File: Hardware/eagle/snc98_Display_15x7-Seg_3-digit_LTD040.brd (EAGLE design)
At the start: 154.9 x 33.5 mm, 72 parts, among them M10 IRLML2244, M11 IRLML2244, M4 IRLML2244, M5 IRLML2244, M6 IRLML2244, M7 IRLML2244, M8 IRLML2244, M9 IRLML2244, X1 MICROMATCH-12, X2 MICROMATCH-14, X3 MICROMATCH-12, X4 MICROMATCH-14

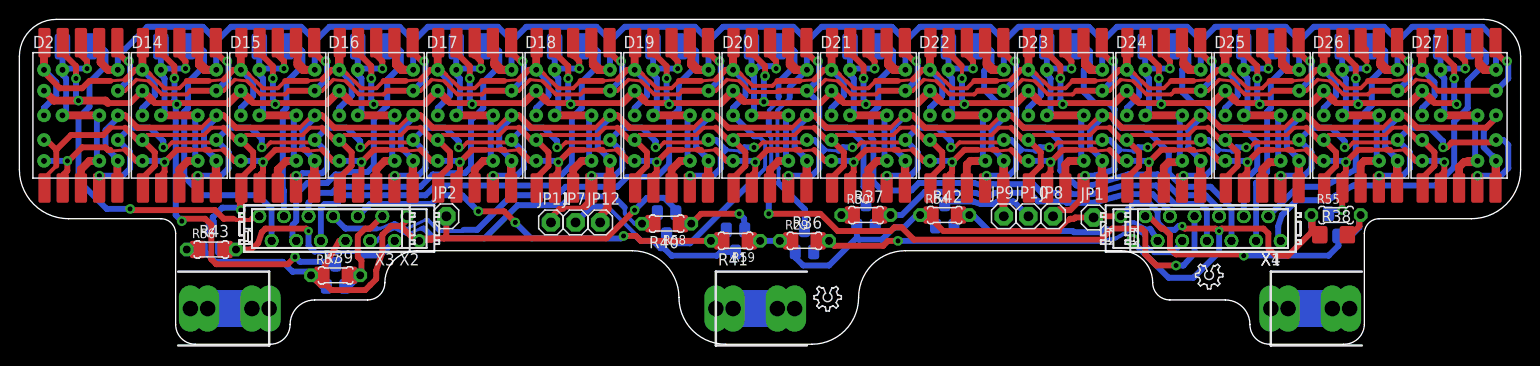
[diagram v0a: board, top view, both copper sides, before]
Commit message: Version 4 mechanical change
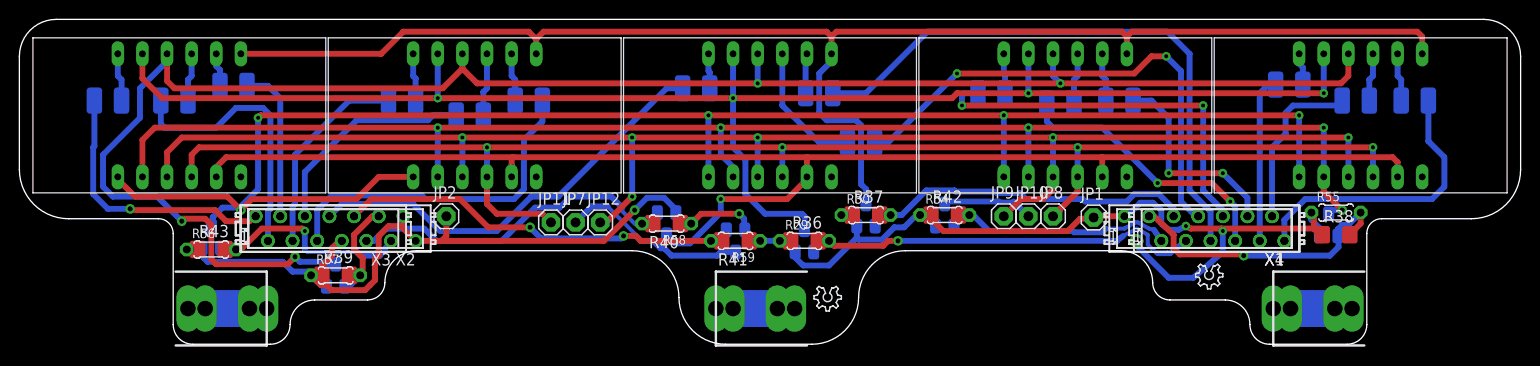
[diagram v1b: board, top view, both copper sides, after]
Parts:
- removed D14, D15, D16, D17, D18, D19, D2, D20, D21, D22, D23, D24, D25, D26, D27: SC40-11_UNISC40-11_UNI, display-hp:10MM_UNI
- added U$1, U$2, U$3, U$4, U$5: LTD040AUE-101A, display_LTD:LTD040AUE-101A
- moved R12 14.0 mm to (86.9, 20.8)
- moved R9 7.11 mm to (46.5, 23.6), turned to 0 degrees
- moved R16 6.91 mm to (113.5, 25.1)
- moved R10 6.91 mm to (52.6, 25.1)
- moved R19 6.91 mm to (144.0, 25.1)
- moved R13 6.65 mm to (82.5, 25.9)
- moved R5 6.49 mm to (9.14, 25.1), turned to 0 degrees
- moved R8 6.43 mm to (39.5, 25.1), turned to 0 degrees
- moved R15 5.84 mm to (107.4, 24.9), turned to 0 degrees
- moved R7 5.75 mm to (22.1, 26.7)
- moved R14 5.71 mm to (100.3, 25.9), turned to 0 degrees
- moved R18 5.59 mm to (137.9, 25.1), turned to 0 degrees
- moved R6 5.59 mm to (16.0, 25.1), turned to 0 degrees
- moved R11 5.29 mm to (69.8, 26.4), turned to 0 degrees
- moved R17 5.14 mm to (131.1, 26.8), turned to 0 degrees
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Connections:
- net DIG_0: now also U$1.12; no longer D2.11, D2.12, D2.13, D2.14, D2.23, D2.28
- net DIG_1: now also U$1.9; no longer D14.11, D14.12, D14.13, D14.14, D14.23, D14.28
- net DIG_10: now also U$4.9; no longer D23.11, D23.12, D23.13, D23.14, D23.23, D23.28
- net DIG_11: now also U$4.8; no longer D24.11, D24.12, D24.13, D24.14, D24.23, D24.28
- net DIG_12: now also U$5.12; no longer D25.11, D25.12, D25.13, D25.14, D25.23, D25.28
- net DIG_13: now also U$5.9; no longer D26.11, D26.12, D26.13, D26.14, D26.23, D26.28
- net DIG_14: now also U$5.8; no longer D27.11, D27.12, D27.13, D27.14, D27.23, D27.28
- net DIG_2: now also U$1.8; no longer D15.11, D15.12, D15.13, D15.14, D15.23, D15.28
- net DIG_3: now also U$2.12; no longer D16.11, D16.12, D16.13, D16.14, D16.23, D16.28
- net DIG_4: now also U$2.9; no longer D17.11, D17.12, D17.13, D17.14, D17.23, D17.28
- net DIG_5: now also U$2.8; no longer D18.11, D18.12, D18.13, D18.14, D18.23, D18.28
- net DIG_6: now also U$3.12; no longer D19.11, D19.12, D19.13, D19.14, D19.23, D19.28
- net DIG_7: now also U$3.9; no longer D20.11, D20.12, D20.13, D20.14, D20.23, D20.28
- net DIG_8: now also U$3.8; no longer D21.11, D21.12, D21.13, D21.14, D21.23, D21.28
- net DIG_9: now also U$4.12; no longer D22.11, D22.12, D22.13, D22.14, D22.23, D22.28
- net SEG_A: now also U$1.11, U$2.11, U$3.11, U$4.11, U$5.11; no longer D14.10, D14.27, D15.10, D15.27, D16.10, D16.27, D17.10, D17.27, D18.10, D18.27, D19.10, D19.27, D2.10, D2.27, D20.10, D20.27, D21.10, D21.27, D22.10, D22.27, D23.10, D23.27, D24.10, D24.27, D25.10, D25.27, D26.10, D26.27, D27.10, D27.27
- net SEG_B: now also U$1.7, U$2.7, U$3.7, U$4.7, U$5.7; no longer D14.26, D14.9, D15.26, D15.9, D16.26, D16.9, D17.26, D17.9, D18.26, D18.9, D19.26, D19.9, D2.26, D2.9, D20.26, D20.9, D21.26, D21.9, D22.26, D22.9, D23.26, D23.9, D24.26, D24.9, D25.26, D25.9, D26.26, D26.9, D27.26, D27.9
- net SEG_C: now also U$1.4, U$2.4, U$3.4, U$4.4, U$5.4; no longer D14.24, D14.7, D15.24, D15.7, D16.24, D16.7, D17.24, D17.7, D18.24, D18.7, D19.24, D19.7, D2.24, D2.7, D20.24, D20.7, D21.24, D21.7, D22.24, D22.7, D23.24, D23.7, D24.24, D24.7, D25.24, D25.7, D26.24, D26.7, D27.24, D27.7
- net SEG_D: now also U$1.2, U$2.2, U$3.2, U$4.2, U$5.2; no longer D14.22, D14.5, D15.22, D15.5, D16.22, D16.5, D17.22, D17.5, D18.22, D18.5, D19.22, D19.5, D2.22, D2.5, D20.22, D20.5, D21.22, D21.5, D22.22, D22.5, D23.22, D23.5, D24.22, D24.5, D25.22, D25.5, D26.22, D26.5, D27.22, D27.5
- net SEG_DP: now also U$1.3, U$2.3, U$3.3, U$4.3, U$5.3; no longer D14.25, D14.6, D14.8, D15.25, D15.6, D15.8, D16.25, D16.6, D16.8, D17.25, D17.6, D17.8, D18.25, D18.6, D18.8, D19.25, D19.6, D19.8, D2.25, D2.6, D2.8, D20.25, D20.6, D20.8, D21.25, D21.6, D21.8, D22.25, D22.6, D22.8, D23.25, D23.6, D23.8, D24.25, D24.6, D24.8, D25.25, D25.6, D25.8, D26.25, D26.6, D26.8, D27.25, D27.6, D27.8
- net SEG_E: now also U$1.1, U$2.1, U$3.1, U$4.1, U$5.1; no longer D14.21, D14.4, D15.21, D15.4, D16.21, D16.4, D17.21, D17.4, D18.21, D18.4, D19.21, D19.4, D2.21, D2.4, D20.21, D20.4, D21.21, D21.4, D22.21, D22.4, D23.21, D23.4, D24.21, D24.4, D25.21, D25.4, D26.21, D26.4, D27.21, D27.4
- net SEG_F: now also U$1.10, U$2.10, U$3.10, U$4.10, U$5.10; no longer D14.2, D14.29, D15.2, D15.29, D16.2, D16.29, D17.2, D17.29, D18.2, D18.29, D19.2, D19.29, D2.2, D2.29, D20.2, D20.29, D21.2, D21.29, D22.2, D22.29, D23.2, D23.29, D24.2, D24.29, D25.2, D25.29, D26.2, D26.29, D27.2, D27.29
- net SEG_G: now also U$1.5, U$2.5, U$3.5, U$4.5, U$5.5; no longer D14.1, D14.3, D14.30, D15.1, D15.3, D15.30, D16.1, D16.3, D16.30, D17.1, D17.3, D17.30, D18.1, D18.3, D18.30, D19.1, D19.3, D19.30, D2.1, D2.3, D2.30, D20.1, D20.3, D20.30, D21.1, D21.3, D21.30, D22.1, D22.3, D22.30, D23.1, D23.3, D23.30, D24.1, D24.3, D24.30, D25.1, D25.3, D25.30, D26.1, D26.3, D26.30, D27.1, D27.3, D27.30
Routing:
- net SEG_G: track 334.8 -> 151.2 mm, vias 0 -> 1
- net SEG_DP: track 332.7 -> 159.4 mm, vias 0 -> 6
- net SEG_A: track 316.3 -> 161.9 mm, vias 0 -> 4
- net SEG_C: track 294.2 -> 152.0 mm, vias 29 -> 4
- net SEG_F: track 306.5 -> 183.9 mm, vias 32 -> 4
- net SEG_B: track 267.4 -> 151.4 mm, vias 15 -> 0
- net SEG_E: track 256.2 -> 174.8 mm, vias 1 -> 5
- net SEG_D: track 207.1 -> 152.9 mm, vias 16 -> 5
- net DIG_13: track 28.8 -> 4.98 mm, vias 1 -> 0
- net DIG_9: track 27.6 -> 4.12 mm, vias 1 -> 0
- net DIG_2: track 26.3 -> 3.46 mm, vias 1 -> 0
- net DIG_6: track 26.3 -> 3.61 mm, vias 1 -> 0
- net DIG_14: track 27.5 -> 4.98 mm, vias 1 -> 0
- net DIG_10: track 27.6 -> 5.24 mm, vias 1 -> 0
- net DIG_8: track 26.3 -> 4.12 mm, vias 1 -> 0
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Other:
- outline, holes or cut-outs redrawn

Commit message: PCB cleaning V1.1
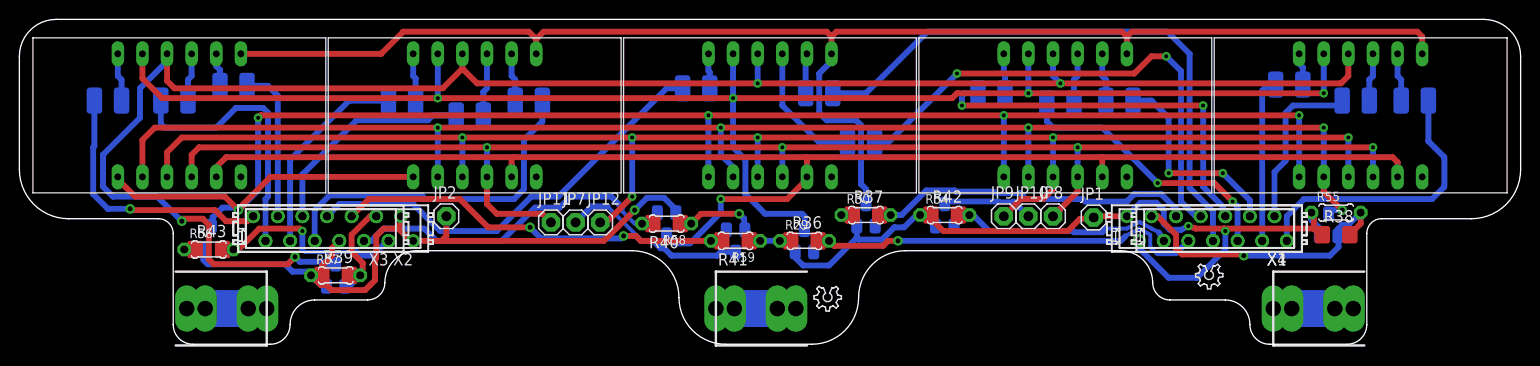
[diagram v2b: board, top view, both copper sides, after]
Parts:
- moved X1 0.25 mm to (123.8, 11.9)
- moved X2 0.25 mm to (32.4, 11.9)
- moved X4 0.25 mm to (122.6, 11.9)
- moved R43 0.25 mm to (19.6, 9.78)
- moved R56 0.25 mm to (19.6, 9.78)
- moved X3 0.25 mm to (31.1, 11.9)
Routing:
- net CA_LED: track 188.3 -> 188.9 mm
- net IO-A: track 43.2 -> 43.7 mm
- net NC3: track 8.13 -> 8.64 mm

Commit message: PCB - add Tear Drop
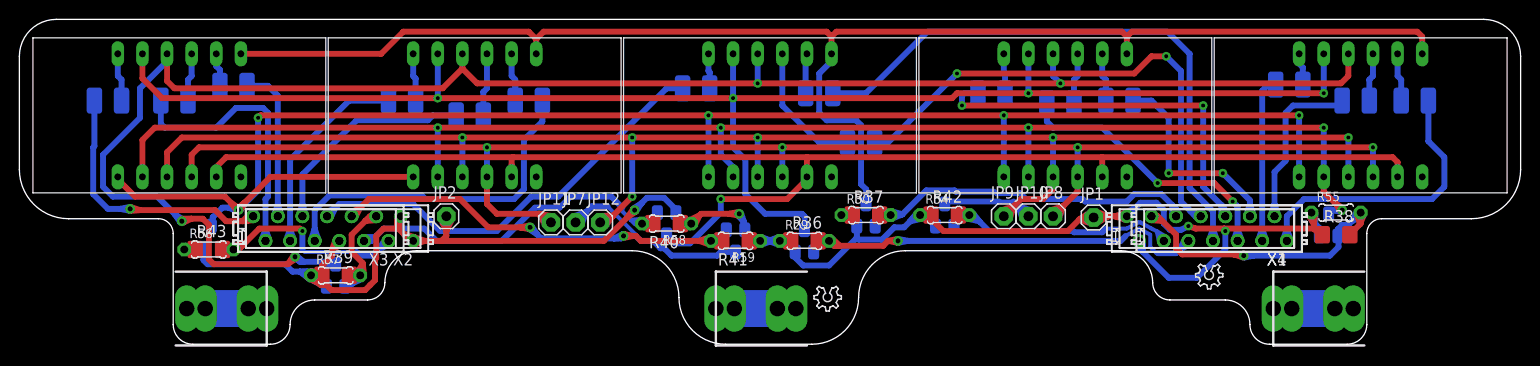
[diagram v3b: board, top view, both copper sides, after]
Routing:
- net CA_LED: track 188.9 -> 294.6 mm
- net IO-DP: track 43.4 -> 62.3 mm
- net IO-A: track 43.7 -> 57.8 mm
- net IO-D: track 30.3 -> 44.4 mm
- net SEG_E: track 174.7 -> 184.3 mm
- net SEG_F: track 183.9 -> 193.5 mm
- net IO-G: track 36.6 -> 46.1 mm
- net IO-C: track 26.0 -> 35.4 mm
- net IO-E: track 22.2 -> 31.6 mm
- net IO-F: track 11.2 -> 20.6 mm
- net IO-B: track 36.4 -> 45.7 mm
- net SEG_DP: track 159.4 -> 167.5 mm
- net SEG_C: track 152.0 -> 160.2 mm
- net D0_A: track 27.7 -> 35.6 mm
- net SEG_D: track 152.9 -> 157.7 mm
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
